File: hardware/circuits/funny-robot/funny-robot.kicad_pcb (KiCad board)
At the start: 2 copper layers, 69.5 x 99 mm, 10 parts, among them J1 To SSD1306OLED, J2 I2C Jumper, U1 Tiny_RTC_DS1307, U2 pca9685 module

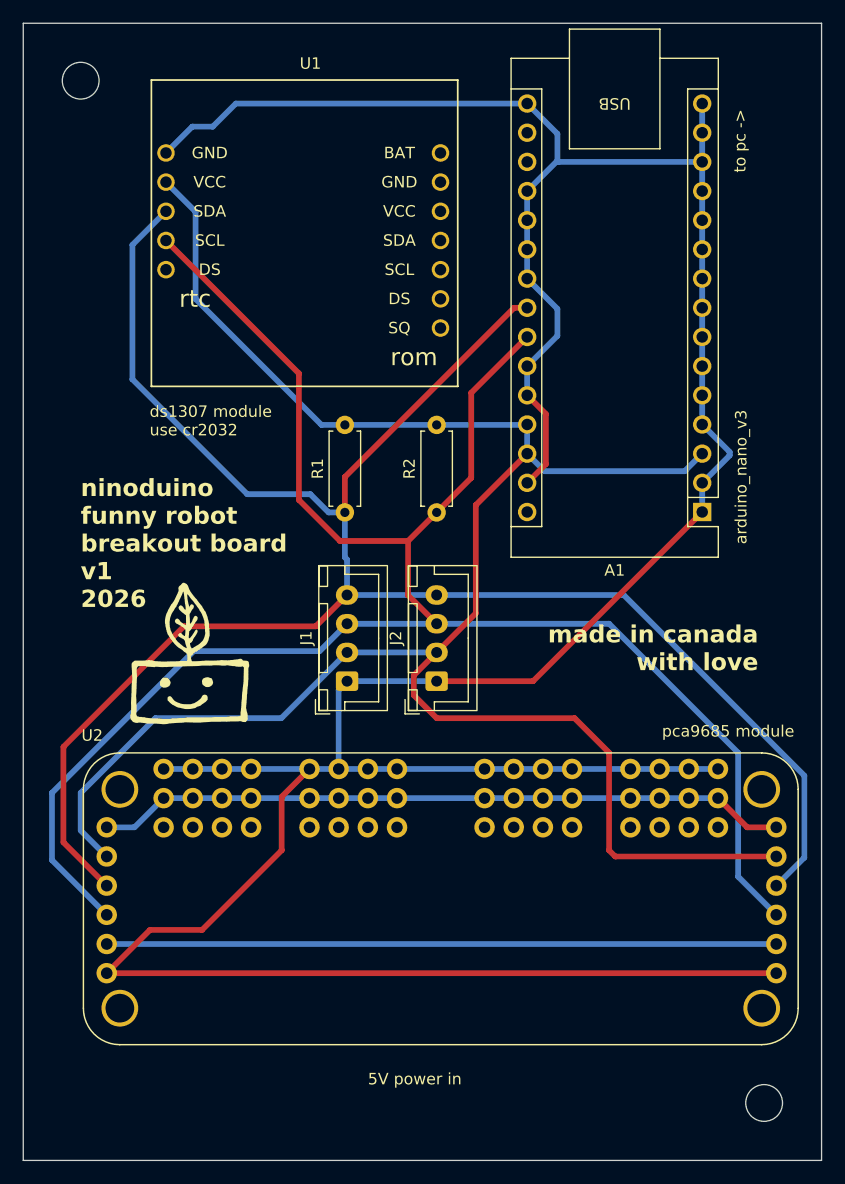
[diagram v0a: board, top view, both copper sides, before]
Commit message: Adjusted logo font and text position
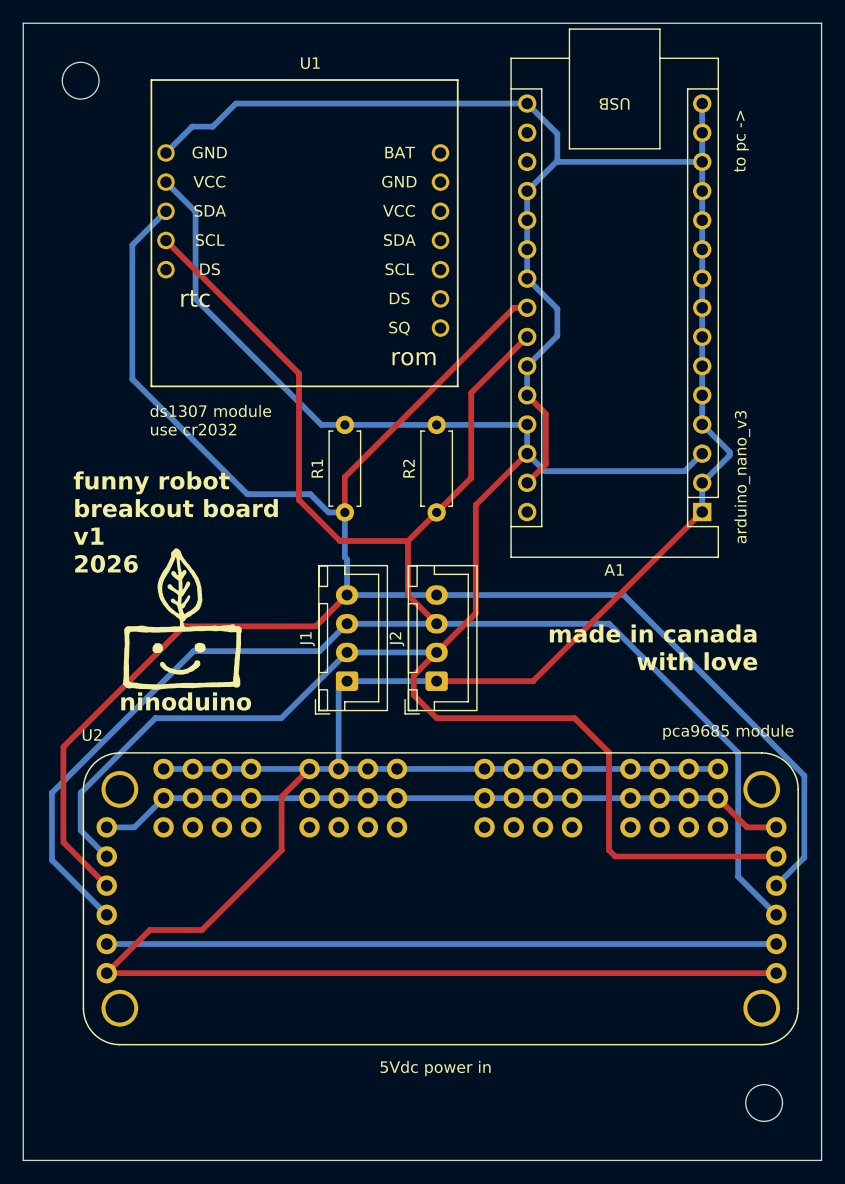
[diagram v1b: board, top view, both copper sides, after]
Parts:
- moved G*** 3.07 mm to (124.0, 99.0)
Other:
- board text added: "5Vdc power in"
- board text added: "funny robot breakout board v1 2026"
- board text added: "ninoduino"
- board text removed: "5V power in"
- board text removed: "ninoduino funny robot breakout board v1 2026"
